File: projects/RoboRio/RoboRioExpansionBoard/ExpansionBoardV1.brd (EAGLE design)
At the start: 100.3 x 80.3 mm, 68 parts, among them IC1 MCP3008, Q1 5MHz

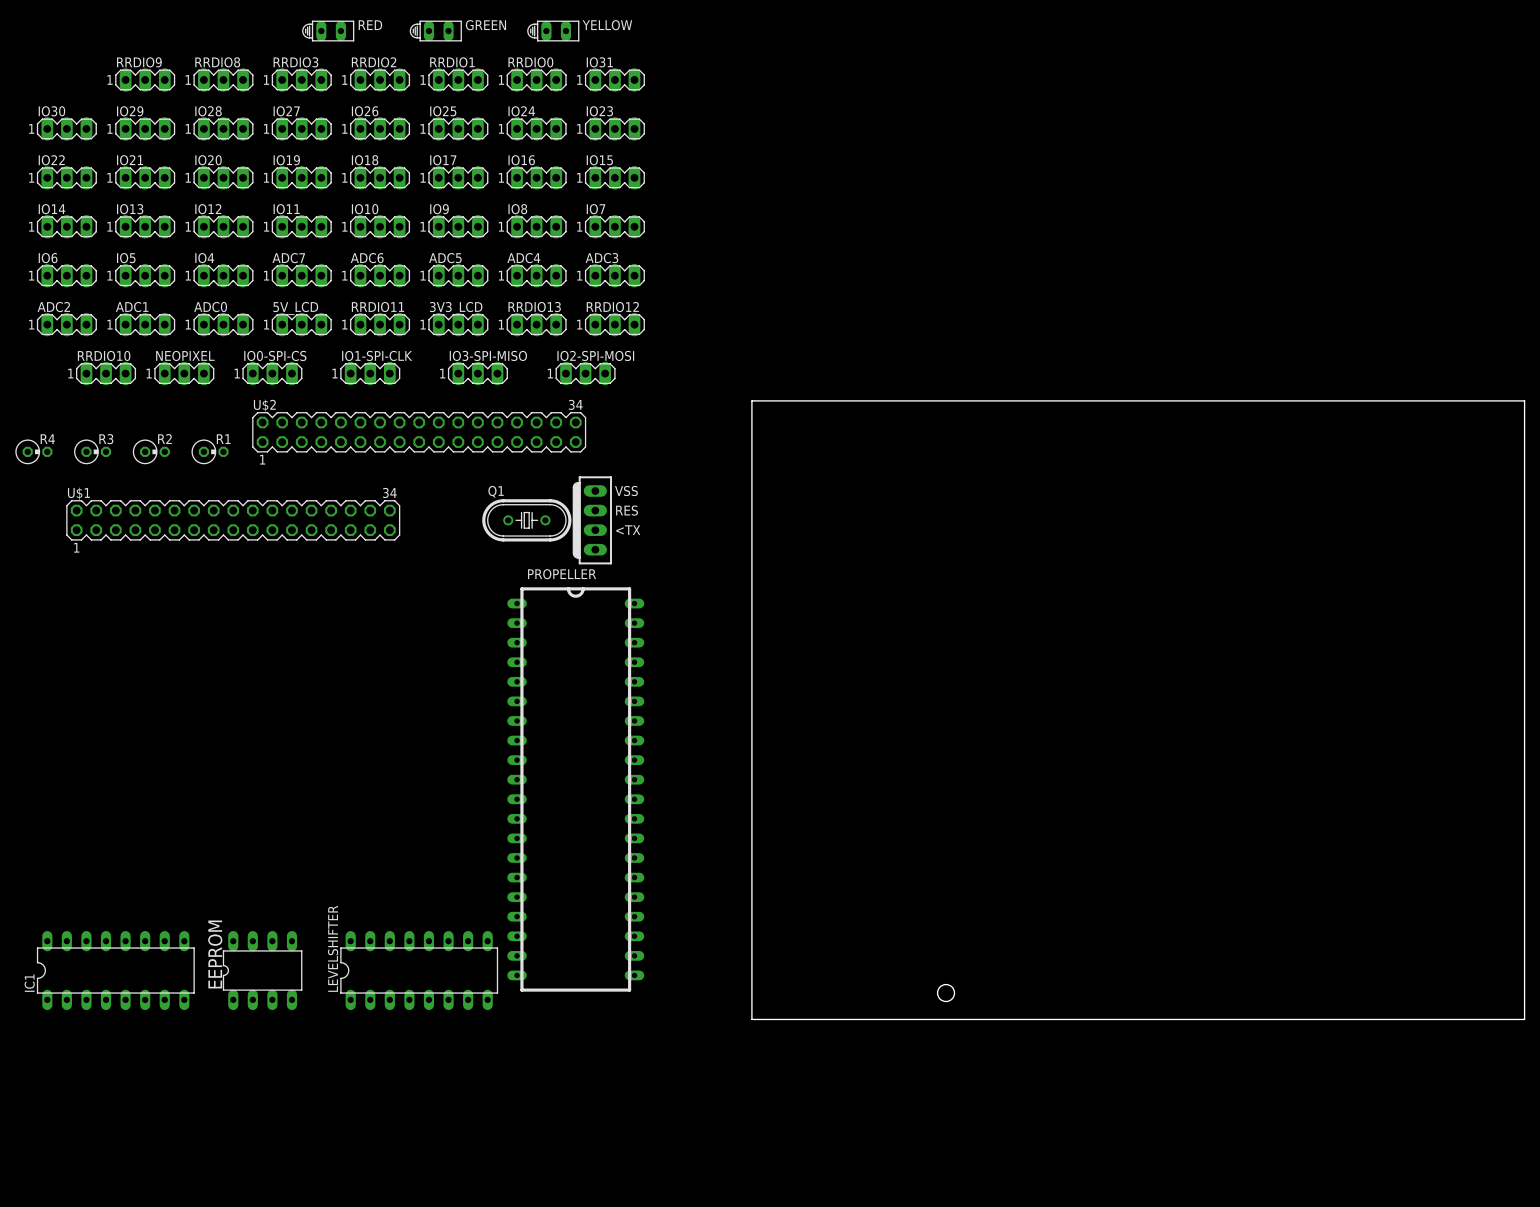
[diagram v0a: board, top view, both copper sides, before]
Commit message: Added RR interface connector
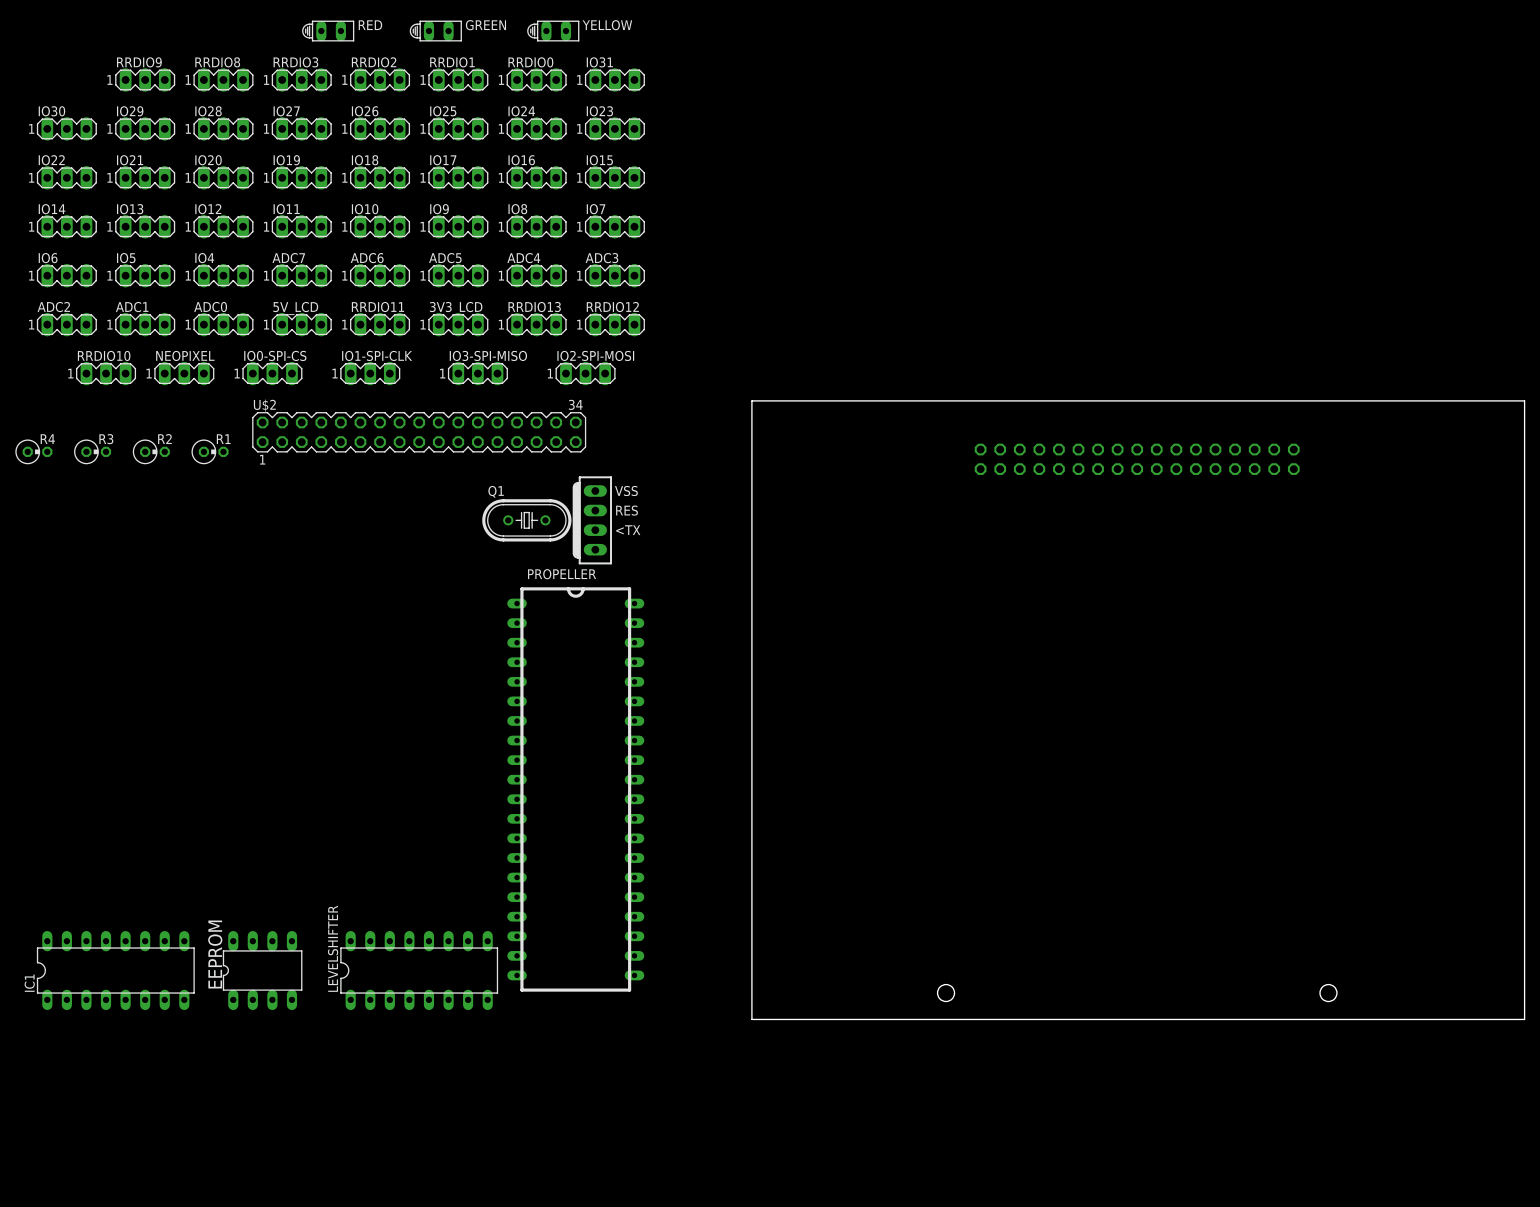
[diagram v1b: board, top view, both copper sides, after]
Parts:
- moved U$1 117.6 mm to (50.0, 72.7), flipped to the bottom

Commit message: Fixed Eric's io pin connections
and added propeller to the board layout
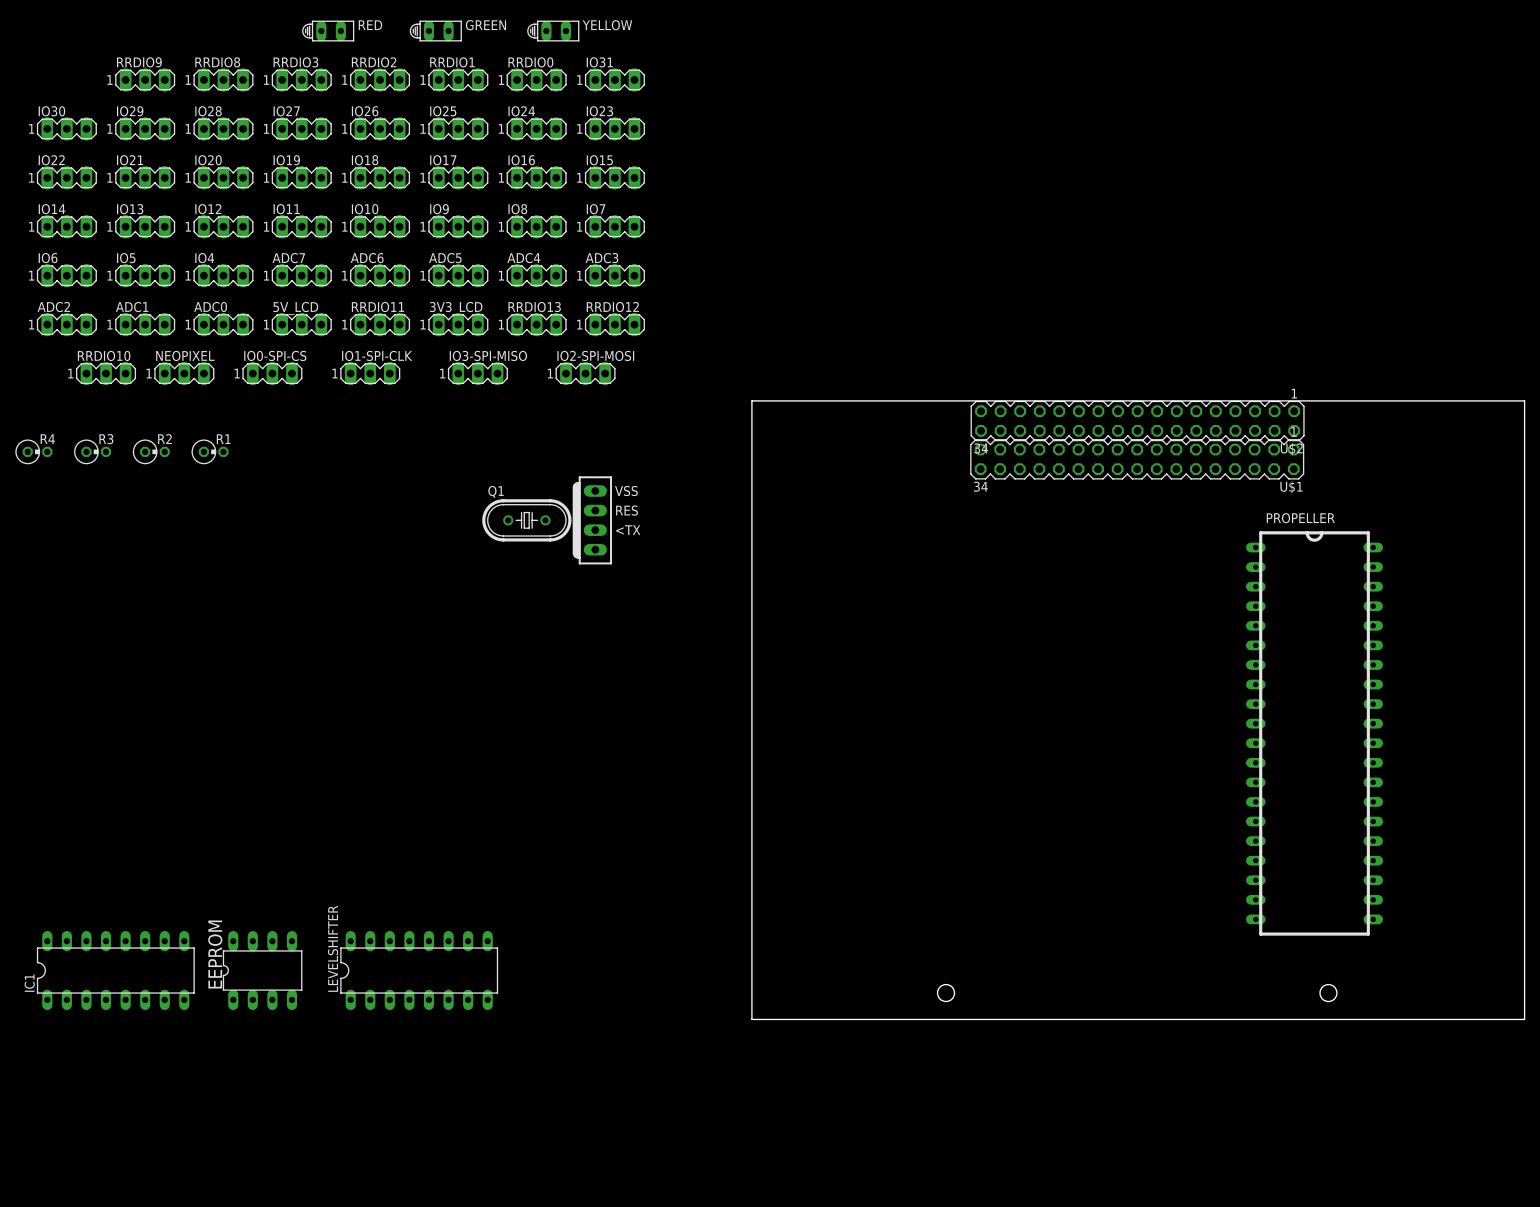
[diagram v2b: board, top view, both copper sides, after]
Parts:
- moved PROPELLER 96.1 mm to (73.0, 37.8)
- moved U$2 93.2 mm to (50.0, 77.7), turned to 180 degrees
- flipped U$1 to the top, turned to 180 degrees
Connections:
- new net IO28: IO28.3
- new net IO29: IO29.3
- new net IO30: IO30.3
- new net IO31: IO31.3
- net +3V3: now also IO0-SPI-CS.2, IO1-SPI-CLK.2, IO10.2, IO11.2, IO12.2, IO13.2, IO14.2, IO15.2, IO16.2, IO17.2, IO18.2, IO19.2, IO2-SPI-MOSI.2, IO20.2, IO21.2, IO22.2, IO23.2, IO24.2, IO25.2, IO26.2, IO27.2, IO28.2, IO29.2, IO3-SPI-MISO.2, IO30.2, IO31.2, IO4.2, IO5.2, IO6.2, IO7.2, IO8.2, IO9.2
- net GND: now also IO10.1, IO11.1, IO12.1, IO13.1, IO14.1, IO15.1, IO16.1, IO17.1, IO18.1, IO19.1, IO21.1, IO22.1, IO23.1, IO24.1, IO25.1, IO26.1, IO27.1, IO28.1, IO29.1, IO30.1, IO8.1, IO9.1
- net IO10: now also IO10.3
- net IO11: now also IO11.3
- net IO14: now also IO14.3
- net IO15: now also IO15.3
- net IO16: now also IO16.3
- net IO17: now also IO17.3
- net IO18: now also IO18.3
- net IO19: now also IO19.3
- net IO20: now also IO20.3
- net IO21: now also IO21.3
- net IO22: now also IO22.3
- net IO23: now also IO23.3
- net IO24: now also IO24.3
- net IO25: now also IO25.3
- net IO26: now also IO26.3
- net IO27: now also IO27.3
- net IO4: now also IO4.3
- net IO5: now also IO5.3
- net IO6: now also IO6.3
- net IO7: now also IO7.3
- net IO8: now also IO8.3
- net IO9: now also IO9.3
- net SPI_CLK: now also IO1-SPI-CLK.3
- net SPI_CS: now also IO0-SPI-CS.3
- net SPI_MISO: now also IO3-SPI-MISO.3
- net SPI_MOSI: now also IO2-SPI-MOSI.3

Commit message: Fixed io 28..31
They were not connected for some reason
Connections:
- removed net IO28: IO28.3
- removed net IO29: IO29.3
- removed net IO30: IO30.3
- removed net IO31: IO31.3
- net SPECIAL28: now also IO28.3
- net SPECIAL29: now also IO29.3
- net SPECIAL30: now also IO30.3
- net SPECIAL31: now also IO31.3
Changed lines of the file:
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@@
 <contactref element="EEPROM" pad="6"/>
 <contactref element="PROPELLER" pad="37"/>
+<contactref element="IO28" pad="3"/>
 <wire x1="-62.23" y1="10.16" x2="80.63" y2="53.625" width="0" layer="19" extent="1-1"/>
+<wire x1="-66.04" y1="115.57" x2="-62.23" y2="10.16" width="0" layer="19" extent="1-1"/>
 </signal>
 <signal name="SPECIAL29">
@@
 <contactref element="R1" pad="1"/>
 <contactref element="PROPELLER" pad="38"/>
+<contactref element="IO29" pad="3"/>
 <wire x1="-59.69" y1="10.16" x2="80.63" y2="56.165" width="0" layer="19" extent="1-1"/>
 <wire x1="-71.12" y1="73.66" x2="-59.69" y2="10.16" width="0" layer="19" extent="1-1"/>
+<wire x1="-76.2" y1="115.57" x2="-71.12" y2="73.66" width="0" layer="19" extent="1-1"/>
 </signal>
 <signal name="SPECIAL30">
 <contactref element="U$3" pad="&gt;RX"/>
 <contactref element="PROPELLER" pad="39"/>
+<contactref element="IO30" pad="3"/>
 <wire x1="-20.32" y1="60.96" x2="80.63" y2="58.705" width="0" layer="19" extent="1-1"/>
+<wire x1="-86.36" y1="115.57" x2="-20.32" y2="60.96" width="0" layer="19" extent="1-1"/>
 </signal>
 <signal name="SPECIAL31">
 <contactref element="U$3" pad="&lt;TX"/>
 <contactref element="PROPELLER" pad="40"/>
+<contactref element="IO31" pad="3"/>
 <wire x1="-20.32" y1="63.5" x2="80.63" y2="61.245" width="0" layer="19" extent="1-1"/>
+<wire x1="-15.24" y1="121.92" x2="-20.32" y2="63.5" width="0" layer="19" extent="1-1"/>
 </signal>
 <signal name="+3V3">
@@
 <wire x1="-55.88" y1="90.17" x2="-41.91" y2="2.54" width="0" layer="19" extent="1-1"/>
 </signal>
-<signal name="IO28">
-<contactref element="IO28" pad="3"/>
-</signal>
-<signal name="IO29">
-<contactref element="IO29" pad="3"/>
-</signal>
-<signal name="IO30">
-<contactref element="IO30" pad="3"/>
-</signal>
-<signal name="IO31">
-<contactref element="IO31" pad="3"/>
-</signal>
 </signals>
